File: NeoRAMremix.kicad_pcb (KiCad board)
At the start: 2 copper layers, 58.2 x 84.1 mm, 29 parts, among them P1 C64-Exp-Port, Q1 2N3904, SW1 Reset, U1 HM628512BFP-5, U2 HM628512BFP-5, U3 HM628512BFP-5, U4 HM628512BFP-5

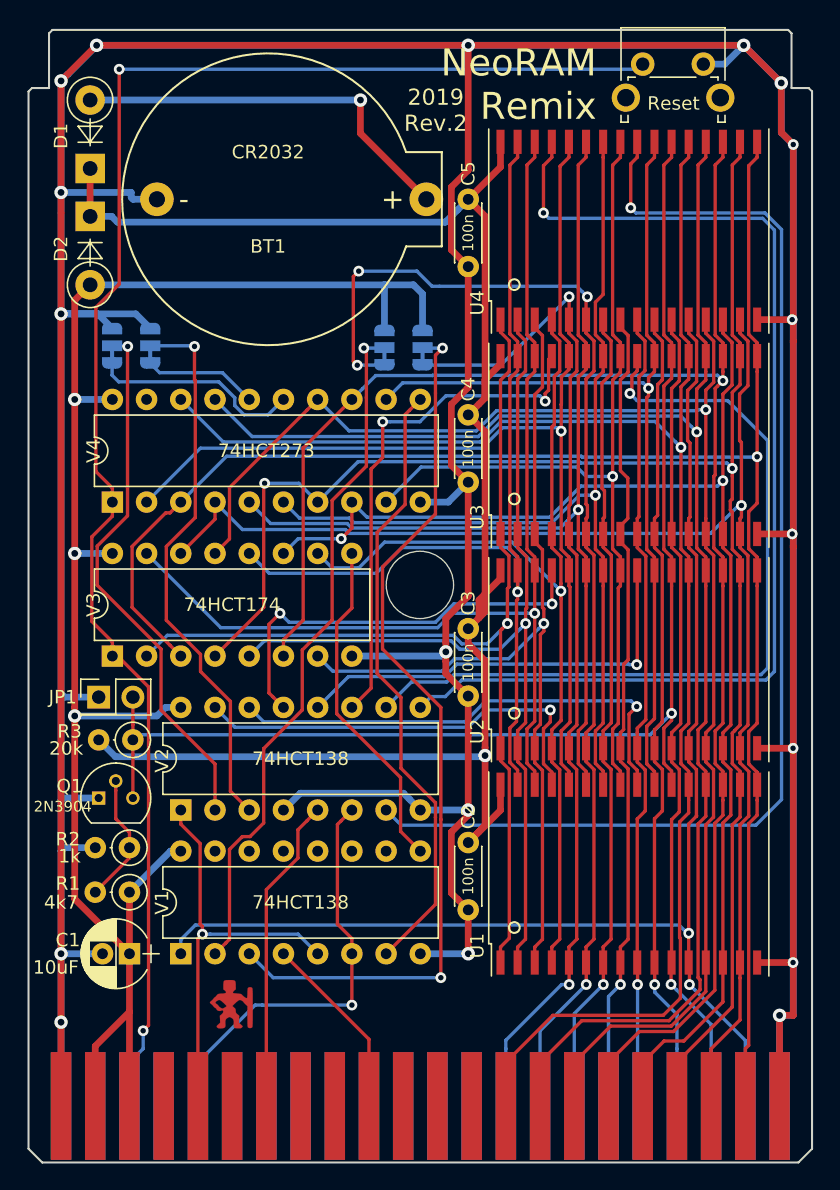
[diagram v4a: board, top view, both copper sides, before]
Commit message: Replaced JP1 with solder jumber SJ5.
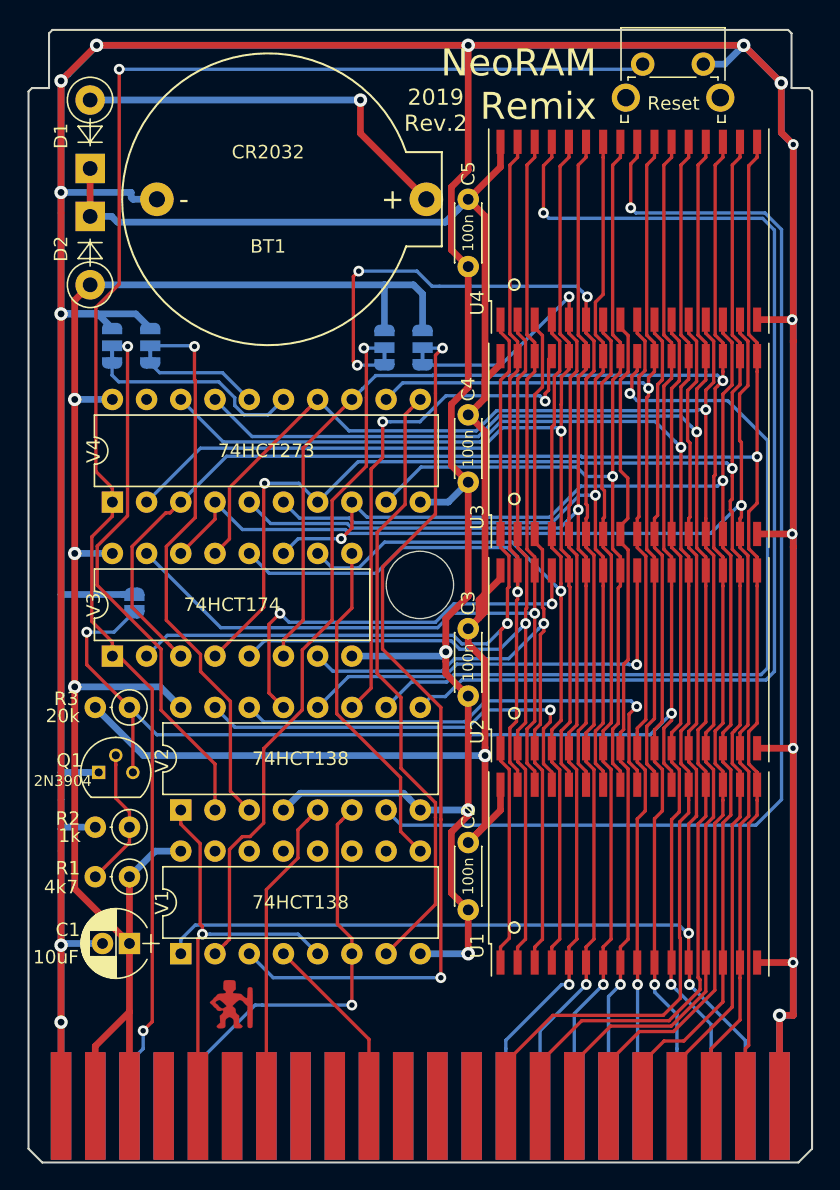
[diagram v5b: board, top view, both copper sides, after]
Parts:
- removed JP1: no_battery, Pin_Headers:Pin_Header_Straight_2x01_Pitch2.54mm
- added SJ5: no_battery, Jumper:SolderJumper-2_P1.3mm_Open_RoundedPad1.0x1.5mm, B.Cu at (91.8, 93.3)
- moved R3 2.43 mm to (91.4, 101.1)
- moved Q1 1.90 mm to (89.2, 105.9)
- moved R2 1.52 mm to (91.4, 110.0)
- moved R1 1.14 mm to (91.4, 113.7)
- moved C1 0.76 mm to (91.4, 118.6)
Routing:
- net Net-(Q1-Pad3): track 97.5 -> 106.9 mm, vias 1 -> 2
- net GND: track 564.9 -> 567.4 mm
- net +BATT: track 130.9 -> 132.2 mm
- net Net-(Q1-Pad2): track 11.0 -> 10.5 mm

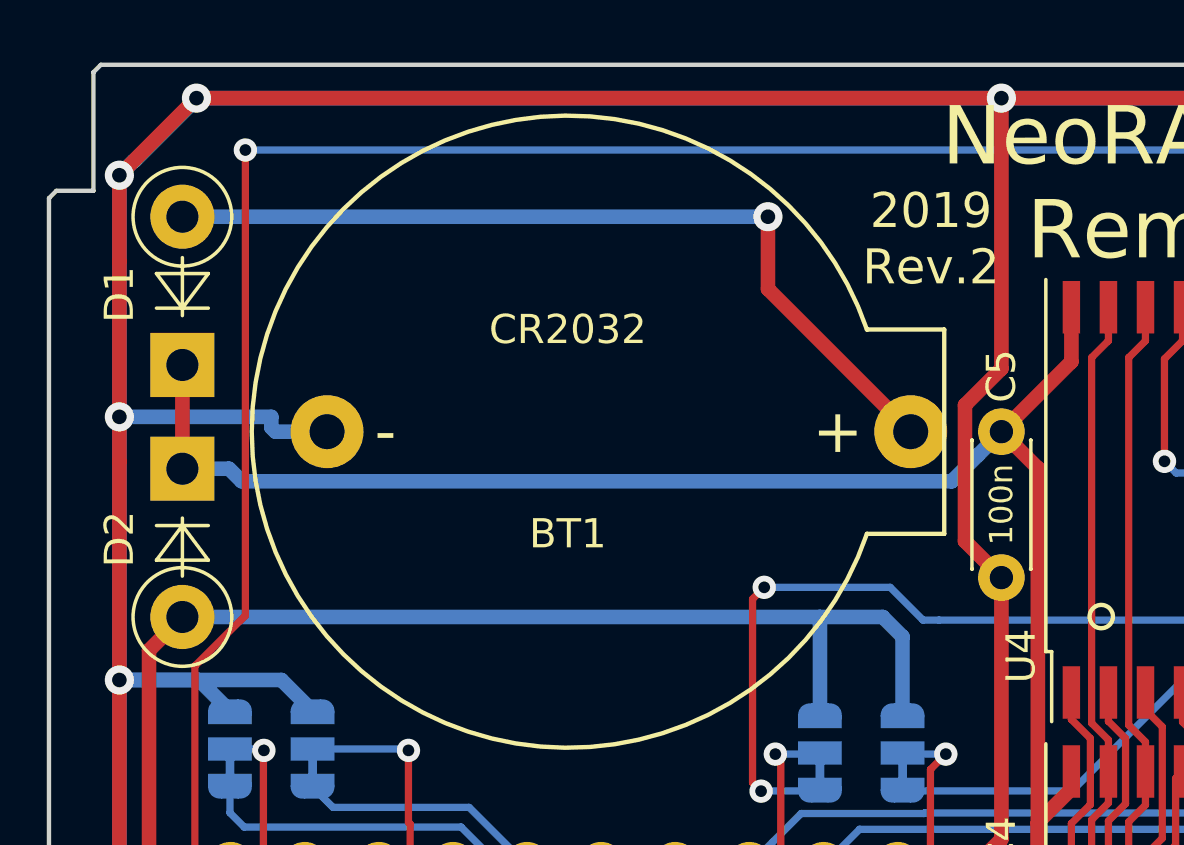
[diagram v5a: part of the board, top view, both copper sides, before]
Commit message: Updated battery holder again.
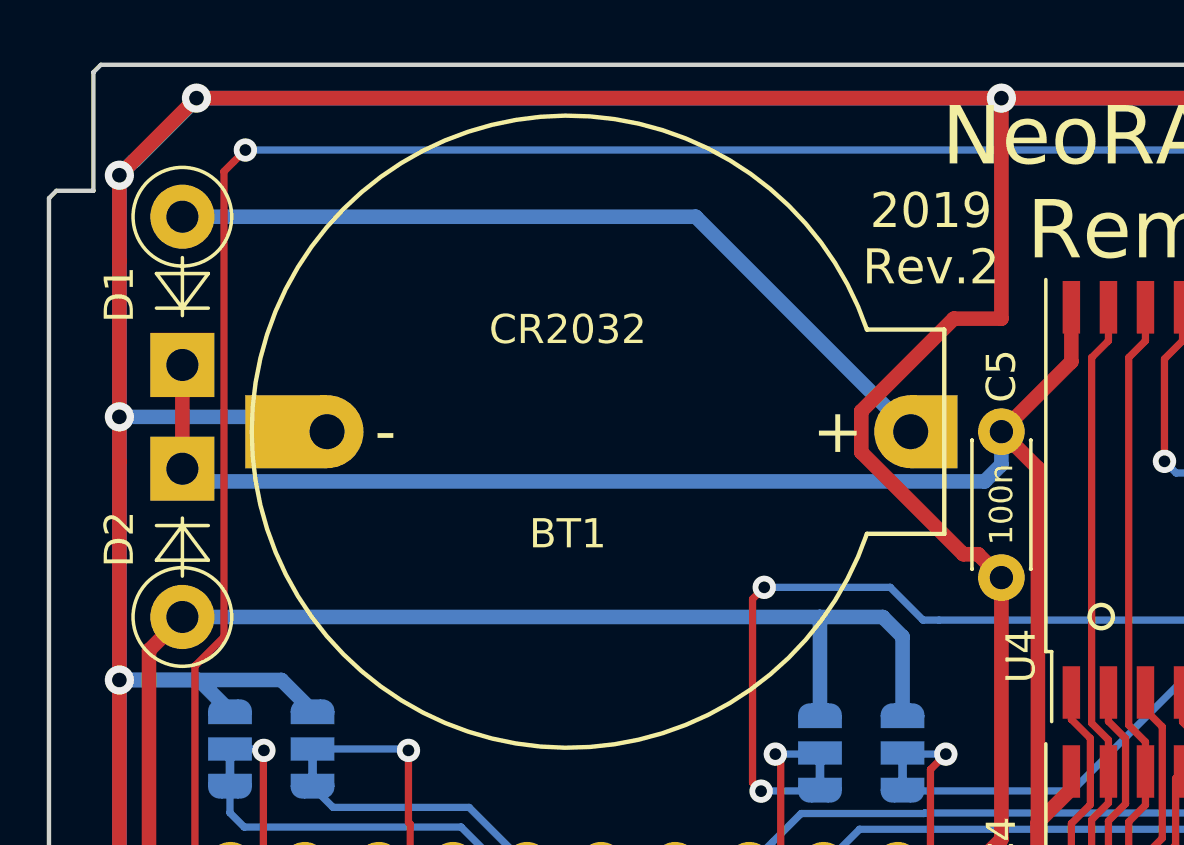
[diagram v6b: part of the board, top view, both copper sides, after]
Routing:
- net GND: track 567.4 -> 571.6 mm
- net Net-(BT1-Pad1): track 29.5 -> 28.0 mm, vias 1 -> 0
- net +BATT: track 132.2 -> 132.9 mm
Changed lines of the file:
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@@
     (thickness 1.6)
     (drawings 21)
-    (tracks 1258)
+    (tracks 1260)
     (zones 0)
     (modules 29)
@@
   (title_block
     (title "NeoRAM Remix")
-    (date 2019-04-28)
-    (rev 2)
+    (date 2019-05-08)
+    (rev 3)
     (company hackup.net)
     (comment 1 "Based on NeoRAM by N. Welte (2007) http://www.1541.de")
@@
     (add_net "Net-(BT1-Pad1)")
   )
+  (module hackup:Battery-Holder-CR2032 locked (layer F.Cu)
+    (at 101.727 63.373)
+    (fp_text reference BT1 (at 0 3.5) (layer F.SilkS)
+      (effects (font (size 1 1) (thickness 0.15)))
+    )
+    (fp_text value CR2032 (at 0 -3.5) (layer F.SilkS)
+      (effects (font (size 1 1) (thickness 0.15)))
+    )
+    (fp_arc (start 0 0) (end 10.599999 -3.749999) (angle -321.0351315) (layer F.CrtYd) (width 0.15))
+    (fp_line (start 13.25 -3.75) (end 10.6 -3.75) (layer F.CrtYd) (width 0.15))
+    (fp_line (start 13.25 3.75) (end 10.6 3.75) (layer F.CrtYd) (width 0.15))
+    (fp_line (start 13.25 -3.75) (end 13.25 3.75) (layer F.CrtYd) (width 0.15))
+    (fp_arc (start 0 0) (end 10.249999 -3.499999) (angle -322.2936825) (layer F.SilkS) (width 0.15))
+    (fp_text user + (at 9.25 0) (layer F.SilkS)
+      (effects (font (size 1.5 1.5) (thickness 0.15)))
+    )
+    (fp_text user - (at -6.25 0) (layer F.SilkS)
+      (effects (font (size 1.5 1.5) (thickness 0.15)))
+    )
+    (fp_line (start 12.9 3.5) (end 10.25 3.5) (layer F.SilkS) (width 0.15))
+    (fp_line (start 12.9 -3.5) (end 12.9 3.5) (layer F.SilkS) (width 0.15))
+    (fp_line (start 10.25 -3.5) (end 12.9 -3.5) (layer F.SilkS) (width 0.15))
+    (pad 1 thru_hole custom (at 11.75 0) (size 2.5 2.5) (drill 1.2) (layers *.Cu *.Mask)
+      (net 2 "Net-(BT1-Pad1)") (zone_connect 0)
+      (options (clearance outline) (anchor circle))
+      (primitives
+        (gr_poly (pts
+           (xy 0 -1.25) (xy 1.6 -1.25) (xy 1.6 1.25) (xy 0 1.25)) (width 0.01))
+      ))
+    (pad 2 thru_hole custom (at -8.25 0) (size 2.5 2.5) (drill 1.2) (layers *.Cu *.Mask)
+      (net 1 GND)
+      (options (clearance outline) (anchor circle))
+      (primitives
+        (gr_poly (pts
+           (xy 0 -1.25) (xy -2.8 -1.25) (xy -2.8 1.25) (xy 0 1.25)) (width 0.01))
+      ))
+  )
   (module NeoRAMremix:C64-Cart-NoSilkS (layer F.Cu)
     (at 83.82 134.62)
@@
       (scale (xyz 0.393701 0.393701 0.393701))
       (rotate (xyz 0 0 0))
-    )
-  )
-  (module hackup:Battery-Holder-CR2032 locked (layer F.Cu)
-    (at 101.727 63.373)
-    (fp_text reference BT1 (at 0 3.5) (layer F.SilkS)
-      (effects (font (size 1 1) (thickness 0.15)))
-    )
-    (fp_text value CR2032 (at 0 -3.5) (layer F.SilkS)
-      (effects (font (size 1 1) (thickness 0.15)))
-    )
-    (fp_arc (start 0 0) (end 10.599999 -3.749999) (angle -321.0351315) (layer F.CrtYd) (width 0.15))
-    (fp_line (start 13.25 -3.75) (end 10.6 -3.75) (layer F.CrtYd) (width 0.15))
-    (fp_line (start 13.25 3.75) (end 10.6 3.75) (layer F.CrtYd) (width 0.15))
-    (fp_line (start 13.25 -3.75) (end 13.25 3.75) (layer F.CrtYd) (width 0.15))
-    (fp_arc (start 0 0) (end 10.249999 -3.499999) (angle -322.2936825) (layer F.SilkS) (width 0.15))
-    (fp_text user + (at 9.25 0) (layer F.SilkS)
-      (effects (font (size 1.5 1.5) (thickness 0.15)))
-    )
-    (fp_text user - (at -6.25 0) (layer F.SilkS)
-      (effects (font (size 1.5 1.5) (thickness 0.15)))
-    )
-    (fp_line (start 12.9 3.5) (end 10.25 3.5) (layer F.SilkS) (width 0.15))
-    (fp_line (start 12.9 -3.5) (end 12.9 3.5) (layer F.SilkS) (width 0.15))
-    (fp_line (start 10.25 -3.5) (end 12.9 -3.5) (layer F.SilkS) (width 0.15))
-    (pad 1 thru_hole circle (at 11.75 0) (size 2.5 2.5) (drill 1.2) (layers *.Cu *.Mask)
-      (net 2 "Net-(BT1-Pad1)"))
-    (pad 2 thru_hole circle (at -8.25 0) (size 2.5 2.5) (drill 1.2) (layers *.Cu *.Mask)
-      (net 1 GND))
-    (model "${KIPRJMOD}/lib/NeoRAMremix.pretty/User Library-CR2032_HOR_HOLD.STEP"
-      (at (xyz 0 0 0))
-      (scale (xyz 1 1 1))
-      (rotate (xyz -90 0 90))
     )
   )
@@
   (segment (start 137.033 51.943) (end 139.827 54.737) (width 0.5) (layer B.Cu) (net 1))
   (segment (start 89.027 51.943) (end 116.586 51.943) (width 0.5) (layer B.Cu) (net 1))
-  (segment (start 116.586 61.214) (end 116.586 51.943) (width 0.5) (layer F.Cu) (net 1))
-  (segment (start 115.335999 62.464001) (end 116.586 61.214) (width 0.5) (layer F.Cu) (net 1))
-  (segment (start 115.335999 67.122999) (end 115.335999 62.464001) (width 0.5) (layer F.Cu) (net 1))
-  (segment (start 116.586 68.373) (end 115.335999 67.122999) (width 0.5) (layer F.Cu) (net 1))
   (segment (start 89.001998 51.943) (end 116.586 51.943) (width 0.5) (layer F.Cu) (net 1))
   (segment (start 116.586 51.943) (end 137.033 51.943) (width 0.5) (layer F.Cu) (net 1))
@@
   (segment (start 86.36 119.38) (end 86.36 118.745) (width 0.5) (layer B.Cu) (net 1))
   (segment (start 86.36 118.745) (end 86.36 111.76) (width 0.5) (layer B.Cu) (net 1))
-  (segment (start 88.519 56.007) (end 108.585 56.007) (width 0.5) (layer B.Cu) (net 2))
-  (via (at 108.585 56.007) (size 1) (drill 0.5) (layers F.Cu B.Cu) (net 2))
-  (segment (start 108.585 58.481) (end 113.477 63.373) (width 0.5) (layer F.Cu) (net 2))
-  (segment (start 108.585 56.007) (end 108.585 58.481) (width 0.5) (layer F.Cu) (net 2))
+  (segment (start 111.783009 62.671324) (end 114.954833 59.4995) (width 0.5) (layer F.Cu) (net 1))
+  (segment (start 111.783009 64.074676) (end 111.783009 62.671324) (width 0.5) (layer F.Cu) (net 1))
+  (segment (start 115.281334 67.573001) (end 111.783009 64.074676) (width 0.5) (layer F.Cu) (net 1))
+  (segment (start 116.586 68.373) (end 115.786001 67.573001) (width 0.5) (layer F.Cu) (net 1))
+  (segment (start 115.786001 67.573001) (end 115.281334 67.573001) (width 0.5) (layer F.Cu) (net 1))
+  (segment (start 114.954833 59.4995) (end 116.586 59.4995) (width 0.5) (layer F.Cu) (net 1))
+  (segment (start 116.586 59.4995) (end 116.586 51.943) (width 0.5) (layer F.Cu) (net 1))
+  (segment (start 106.111 56.007) (end 113.477 63.373) (width 0.5) (layer B.Cu) (net 2))
+  (segment (start 88.519 56.007) (end 106.111 56.007) (width 0.5) (layer B.Cu) (net 2))
   (segment (start 88.9 126.238) (end 91.44 123.698) (width 0.5) (layer F.Cu) (net 3))
   (segment (start 88.9 130.681726) (end 88.9 126.238) (width 0.5) (layer F.Cu) (net 3))
@@
   (segment (start 117.836001 97.631371) (end 117.836001 104.0765) (width 0.5) (layer F.Cu) (net 4))
   (segment (start 117.836001 104.0765) (end 117.836001 109.874999) (width 0.5) (layer F.Cu) (net 4))
-  (segment (start 115.786001 64.172999) (end 116.586 63.373) (width 0.5) (layer B.Cu) (net 4))
-  (segment (start 114.885999 65.073001) (end 115.786001 64.172999) (width 0.5) (layer B.Cu) (net 4))
-  (segment (start 90.549001 65.073001) (end 114.885999 65.073001) (width 0.5) (layer B.Cu) (net 4))
-  (segment (start 88.519 64.643) (end 90.119 64.643) (width 0.5) (layer B.Cu) (net 4))
-  (segment (start 90.119 64.643) (end 90.549001 65.073001) (width 0.5) (layer B.Cu) (net 4))
   (via (at 117.836001 104.667999) (size 1) (drill 0.5) (layers F.Cu B.Cu) (net 4))
   (segment (start 117.748999 104.755001) (end 117.836001 104.667999) (width 0.5) (layer B.Cu) (net 4))
   (segment (start 92.475999 104.667999) (end 117.836001 104.667999) (width 0.5) (layer B.Cu) (net 4))
   (segment (start 88.9 101.092) (end 92.475999 104.667999) (width 0.5) (layer B.Cu) (net 4))
+  (segment (start 116.586 64.50437) (end 116.586 63.373) (width 0.5) (layer B.Cu) (net 4))
+  (segment (start 116.01236 65.07801) (end 116.586 64.50437) (width 0.5) (layer B.Cu) (net 4))
+  (segment (start 88.519 64.643) (end 88.95401 65.07801) (width 0.5) (layer B.Cu) (net 4))
+  (segment (start 88.95401 65.07801) (end 116.01236 65.07801) (width 0.5) (layer B.Cu) (net 4))
   (via (at 96.854068 117.925011) (size 0.8) (drill 0.4) (layers F.Cu B.Cu) (net 5))
   (segment (start 96.52 118.259079) (end 96.854068 117.925011) (width 0.25) (layer F.Cu) (net 5))
@@
   (segment (start 90.17 85.852) (end 90.17 86.902) (width 0.25) (layer F.Cu) (net 16))
   (segment (start 90.17 96.232) (end 90.17 97.282) (width 0.25) (layer F.Cu) (net 16))
-  (segment (start 88.947995 71.403007) (end 90.678 69.673002) (width 0.25) (layer F.Cu) (net 16))
   (segment (start 88.947995 83.579995) (end 88.947995 71.403007) (width 0.25) (layer F.Cu) (net 16))
   (segment (start 90.17 85.852) (end 90.17 84.802) (width 0.25) (layer F.Cu) (net 16))
   (segment (start 90.17 84.802) (end 88.947995 83.579995) (width 0.25) (layer F.Cu) (net 16))
   (via (at 90.678 53.721) (size 0.8) (drill 0.4) (layers F.Cu B.Cu) (net 16))
-  (segment (start 90.678 69.673002) (end 90.678 53.721) (width 0.25) (layer F.Cu) (net 16))
   (segment (start 129.159 53.721) (end 129.54 53.34) (width 0.25) (layer B.Cu) (net 16))
   (segment (start 90.678 53.721) (end 129.159 53.721) (width 0.25) (layer B.Cu) (net 16))
@@
   (segment (start 93.131002 124.419998) (end 93.131002 99.751998) (width 0.25) (layer F.Cu) (net 16))
   (segment (start 92.456 125.095) (end 93.131002 124.419998) (width 0.25) (layer F.Cu) (net 16))
+  (segment (start 90.278001 54.120999) (end 90.678 53.721) (width 0.25) (layer F.Cu) (net 16))
+  (segment (start 89.944001 54.454999) (end 90.278001 54.120999) (width 0.25) (layer F.Cu) (net 16))
+  (segment (start 88.947995 71.403007) (end 89.944001 70.407001) (width 0.25) (layer F.Cu) (net 16))
+  (segment (start 89.944001 70.407001) (end 89.944001 54.454999) (width 0.25) (layer F.Cu) (net 16))
   (via (at 107.95 123.19) (size 0.8) (drill 0.4) (layers F.Cu B.Cu) (net 17))
   (segment (start 101.294724 123.19) (end 107.95 123.19) (width 0.25) (layer B.Cu) (net 17))

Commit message: Updated battery holder again.
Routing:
- net GND: track 571.6 -> 568.7 mm
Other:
- board text added: "2019 Rev.3"
- board text removed: "2019 Rev.2"
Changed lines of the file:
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@@
   (gr_line (start 83.947 55.372) (end 84.201 55.118) (layer Edge.Cuts) (width 0.15))
   (gr_line (start 83.82 50.8) (end 142.24 50.8) (layer Eco1.User) (width 0.2))
-  (gr_text "2019\nRev.2" (at 114.173 56.769) (layer F.SilkS)
+  (gr_text "2019\nRev.3" (at 114.173 56.769) (layer F.SilkS)
     (effects (font (size 1.2 1.2) (thickness 0.25)))
   )
@@
   (segment (start 137.033 51.943) (end 139.827 54.737) (width 0.5) (layer B.Cu) (net 1))
   (segment (start 89.027 51.943) (end 116.586 51.943) (width 0.5) (layer B.Cu) (net 1))
-  (segment (start 89.001998 51.943) (end 116.586 51.943) (width 0.5) (layer F.Cu) (net 1))
   (segment (start 116.586 51.943) (end 137.033 51.943) (width 0.5) (layer F.Cu) (net 1))
   (segment (start 116.586 51.943) (end 137.033 51.943) (width 0.5) (layer B.Cu) (net 1))
-  (via (at 116.586 51.943) (size 1) (drill 0.5) (layers F.Cu B.Cu) (net 1))
   (via (at 137.033 51.943) (size 1) (drill 0.5) (layers F.Cu B.Cu) (net 1))
   (segment (start 134.04 53.34) (end 135.636 53.34) (width 0.5) (layer B.Cu) (net 1))
@@
   (segment (start 86.36 119.38) (end 86.36 118.745) (width 0.5) (layer B.Cu) (net 1))
   (segment (start 86.36 118.745) (end 86.36 111.76) (width 0.5) (layer B.Cu) (net 1))
-  (segment (start 111.783009 62.671324) (end 114.954833 59.4995) (width 0.5) (layer F.Cu) (net 1))
-  (segment (start 111.783009 64.074676) (end 111.783009 62.671324) (width 0.5) (layer F.Cu) (net 1))
-  (segment (start 115.281334 67.573001) (end 111.783009 64.074676) (width 0.5) (layer F.Cu) (net 1))
+  (segment (start 111.783009 52.046991) (end 111.887 51.943) (width 0.5) (layer F.Cu) (net 1))
+  (segment (start 111.887 51.943) (end 116.586 51.943) (width 0.5) (layer F.Cu) (net 1))
+  (segment (start 89.001998 51.943) (end 111.8235 51.943) (width 0.5) (layer F.Cu) (net 1))
   (segment (start 116.586 68.373) (end 115.786001 67.573001) (width 0.5) (layer F.Cu) (net 1))
   (segment (start 115.786001 67.573001) (end 115.281334 67.573001) (width 0.5) (layer F.Cu) (net 1))
-  (segment (start 114.954833 59.4995) (end 116.586 59.4995) (width 0.5) (layer F.Cu) (net 1))
-  (segment (start 116.586 59.4995) (end 116.586 51.943) (width 0.5) (layer F.Cu) (net 1))
+  (segment (start 115.281334 67.573001) (end 111.783009 64.074676) (width 0.5) (layer F.Cu) (net 1))
+  (segment (start 111.783009 64.074676) (end 111.783009 52.046991) (width 0.5) (layer F.Cu) (net 1))
+  (segment (start 111.8235 51.943) (end 111.887 51.943) (width 0.5) (layer F.Cu) (net 1))
+  (via (at 111.8235 51.943) (size 1) (drill 0.5) (layers F.Cu B.Cu) (net 1))
   (segment (start 106.111 56.007) (end 113.477 63.373) (width 0.5) (layer B.Cu) (net 2))
   (segment (start 88.519 56.007) (end 106.111 56.007) (width 0.5) (layer B.Cu) (net 2))

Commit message: Fixed revision number on bottom side.
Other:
- board text added: "NeoRAM Remix Rev.3 https://github.com/hackup/NeoRAMremix Original design (2007): http://www.x1541.de/ Remix (2019): https://www.hackup.net/"
- board text removed: "NeoRAM Remix Rev.2 https://github.com/hackup/NeoRAMremix Original design (2007): http://www.x1541.de/ Remix (2019): https://www.hackup.net/"
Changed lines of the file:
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@@
-(kicad_pcb (version 20171130) (host pcbnew "(5.1.0)-1")
+(kicad_pcb (version 20171130) (host pcbnew "(5.1.5)-3")
   (general
     (thickness 1.6)
@@
       (net 53 "Net-(SJ4-Pad2)"))
   )
-  (gr_text "NeoRAM Remix Rev.2\nhttps://github.com/hackup/NeoRAMremix\nOriginal design (2007): http://www.x1541.de/\nRemix (2019): https://www.hackup.net/" (at 134.62 120.523 270) (layer B.SilkS)
+  (gr_text "NeoRAM Remix Rev.3\nhttps://github.com/hackup/NeoRAMremix\nOriginal design (2007): http://www.x1541.de/\nRemix (2019): https://www.hackup.net/" (at 134.62 120.523 270) (layer B.SilkS)
     (effects (font (size 1.5 1.5) (thickness 0.3)) (justify left mirror))
   )
